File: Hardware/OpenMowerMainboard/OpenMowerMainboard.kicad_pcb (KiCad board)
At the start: 2 copper layers, 247.1 x 170 mm, 174 parts, among them IC1 74ALVC164245DGG,11, IC2 TSC101CILT, IC3 MAX20405AFOF_VY+T, J1 Conn_02x11_Top_Bottom, J10 Conn_01x05, J11 Conn_01x03_Male, J12 Conn_01x03_Male, J13 Conn_01x03_Male, J14 Conn_01x03_Male, J16 Conn_01x08, J17 Conn_01x02, J18 Conn_01x02, J19 Conn_01x04, J2 Conn_02x04_Top_Bottom, J20 Conn_01x10_Female, J21 Raspberry_Pi_2_3, J22 Conn_02x04_Odd_Even, J23 Conn_01x08, J3 Conn_01x02, J4 Conn_01x05, J5 Conn_01x04, J6 Conn_01x04, J7 Conn_01x04, J8 Conn_01x04, J9 Conn_01x04, M1 Fan, Q13 BSS138, Q14 BSS138, Q15 BSS138, Q16 BSS138, Q3 BSS138, Q5 BSS138, Q6 Q_PMOS_GDS, SW1 MK-11C04-G013, SW2 DA-01BP, U1 DNP, U10 74HC4051, U11 Pico, U2 MCP604, U3 SIP32509DT, U4 xESC2, U5 xESC2, U6 xESC2, U7 SN74LV1T34DBV, U9 74HC4051

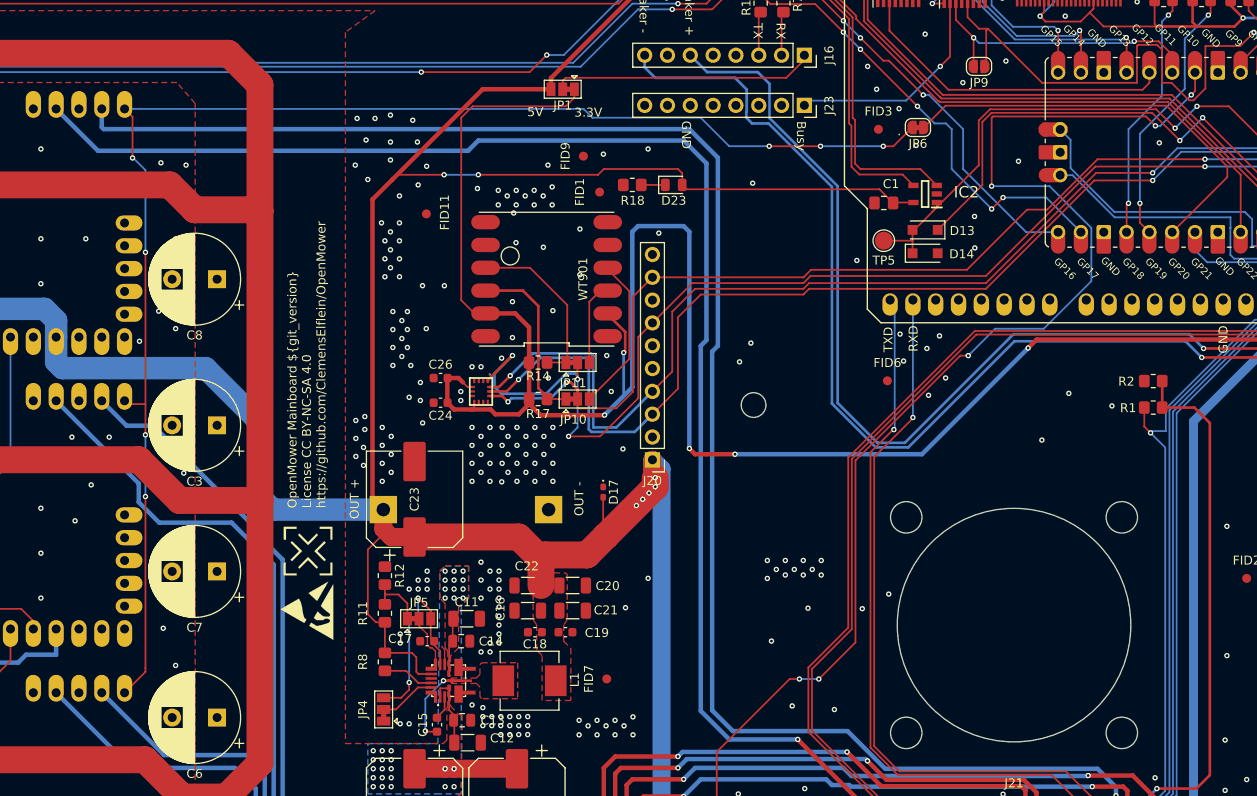
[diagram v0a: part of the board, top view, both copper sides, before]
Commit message: mainboard: fix J16-J23 distance
Make distance between J16 and J23 fit the DFplayer again
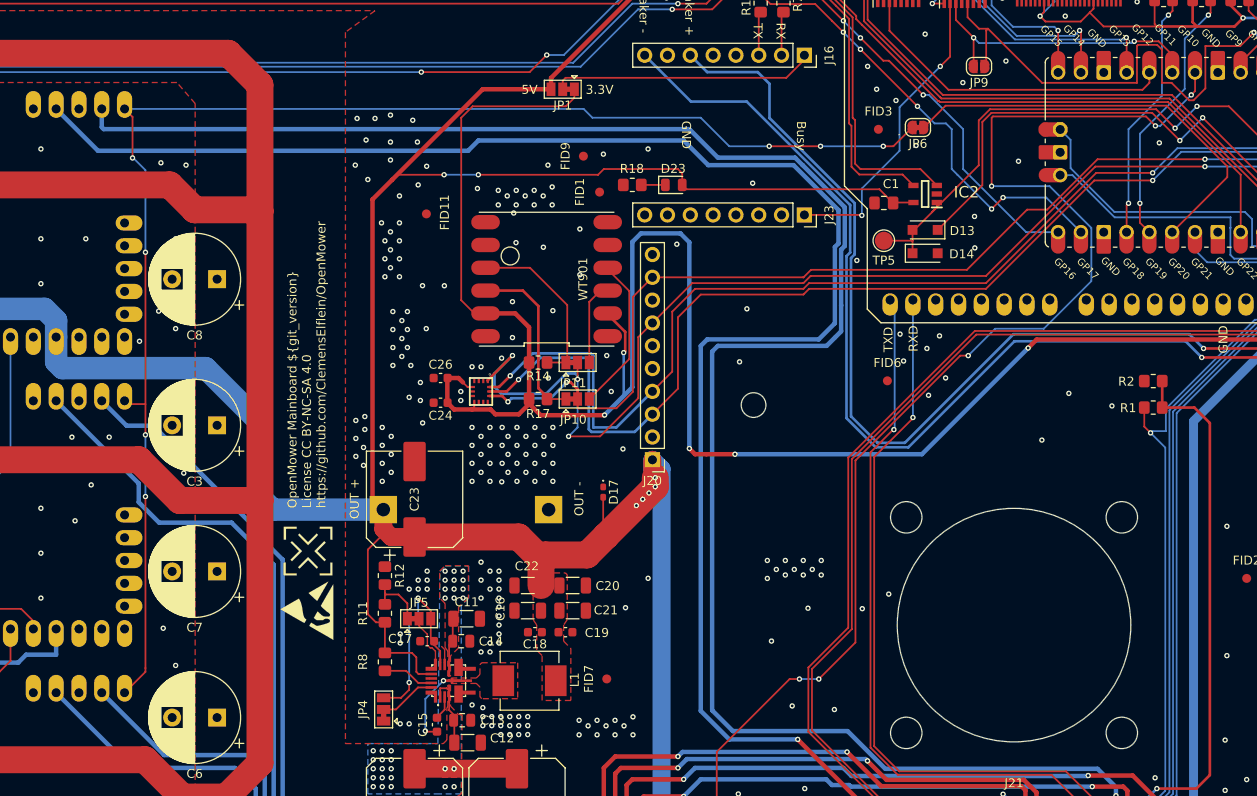
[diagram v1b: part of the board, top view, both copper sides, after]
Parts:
- moved J23 12.2 mm to (222.8, 82.7)
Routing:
- net /ESCs/MR_RX: track 161.2 -> 186.2 mm
- net /ESCs/MR_TX: track 184.9 -> 208.7 mm
- net /pico/SOUND_BUSY: track 24.4 -> 34.1 mm, vias 1 -> 2
- net /RobotConnectors/SPEAKER_MINUS: track 203.8 -> 201.4 mm
- net +3V3: track 548.4 -> 546.4 mm

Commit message: mainboard: landroid battery connector
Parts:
- removed J2: Conn_02x04_Top_Bottom, Connector_Molex:Molex_Mini-Fit_Jr_5566-08A_2x04_P4.20mm_Vertical
- added J51: Conn_01x04, Connector_Molex:Molex_Mini-Fit_Jr_5566-04A_2x02_P4.20mm_Vertical, F.Cu at (77.5, 98.1)
- moved FID16 27.0 mm to (72.0, 100.0), turned to 0 degrees
- moved C14 0.49 mm to (184.1, 130.4)
- moved C17 0.49 mm to (180.3, 130.4)
- moved C18 0.49 mm to (192.3, 129.4)
- moved C25 0.49 mm to (211.6, 160.2)
- moved J22 0.49 mm to (240.4, 165.2)
- moved U7 0.49 mm to (211.8, 164.7)
- moved C1 0.49 mm to (231.2, 81.6)
- moved C16 0.49 mm to (191.5, 127.0)
- moved C20 0.49 mm to (196.5, 124.2)
- moved C21 0.49 mm to (196.5, 127.0)
- moved C22 0.49 mm to (191.5, 124.2)
- moved D13 0.49 mm to (235.8, 84.6)
- moved D17 0.49 mm to (199.9, 113.8)
- moved D2 0.49 mm to (80.7, 73.2)
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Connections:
- Q6 pad 2: /RobotConnectors/MosfetSwitch/VOUT -> /RobotConnectors/V_BATTERY
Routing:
- net /RobotConnectors/V_BATTERY: track 205.9 -> 292.1 mm
- net /RobotConnectors/MosfetSwitch/VOUT: track 25.7 -> 0.00 mm
- net Net-(J51-Pin_4): track 44.0 -> 28.6 mm
- net Net-(J2-Pin_1): track 14.0 -> 0.00 mm
- net /RobotConnectors/V_CHARGE: track 257.5 -> 269.6 mm, vias 0 -> 1
- net Net-(J3-Pin_2): track 19.1 -> 28.7 mm
- net V_BATT: track 442.7 -> 445.9 mm
- net GND: vias 589 -> 595
